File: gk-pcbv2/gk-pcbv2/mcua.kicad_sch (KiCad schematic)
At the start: 23 parts, among them J14 Conn_01x02, SW1 SW_Push, U4 STM32H747BITx, Y1 16MHz, Y2 32.768kHz R26-32.768-12.5

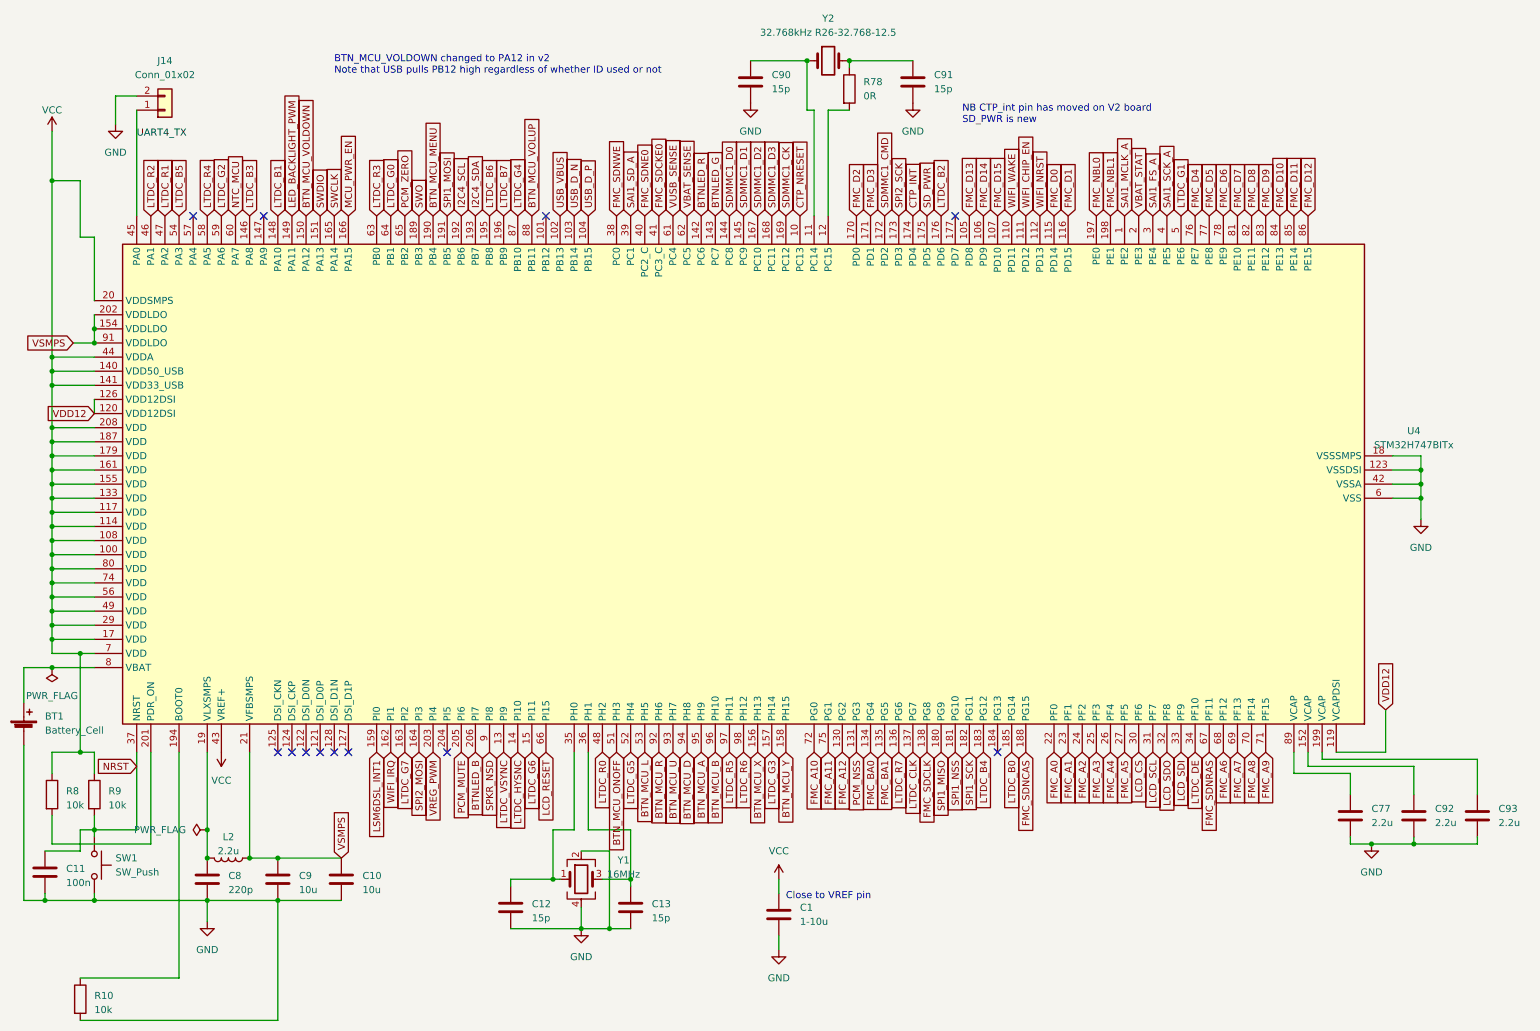
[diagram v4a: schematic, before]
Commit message: PCB updates - add xbox joystick
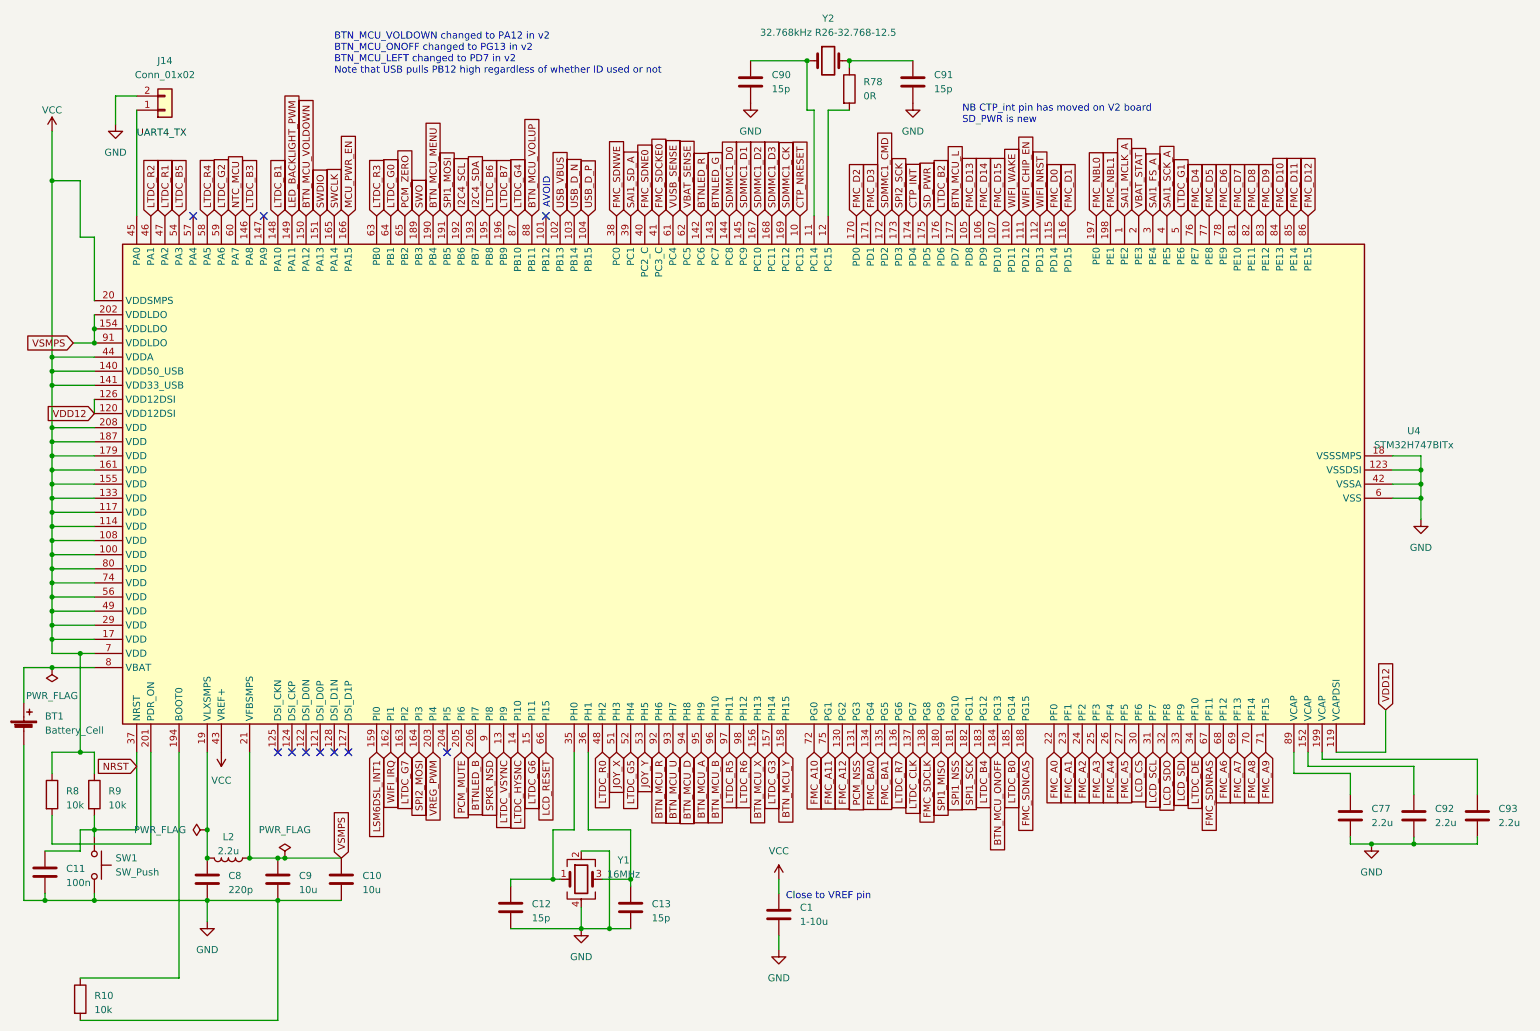
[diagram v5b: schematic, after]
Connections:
- net BTN_MCU_L: now also U4.177 (PD7); no longer U4.53 (PH5)
- net BTN_MCU_ONOFF: now also U4.184 (PG13); no longer U4.51 (PH3)
- new net JOY_X: U4.51 (PH3)
- new net JOY_Y: U4.53 (PH5)
- no-connect marks 12 -> 10
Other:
- note added: "AVOID"
- note added: "BTN_MCU_VOLDOWN changed to PA12 in v2 BTN_MCU_ONOFF changed to PG13 in v2 BTN_MCU_LEFT changed to PD7 in v2 Note that USB pulls PB12 high regardless of whether ID used or not"
- note removed: "BTN_MCU_VOLDOWN changed to PA12 in v2 Note that USB pulls PB12 high regardless of whether ID used or not"
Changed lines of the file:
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@@
   (junction (at 20.32 110.49) (diameter 0) (color 0 0 0 0)
+  )
+  (junction (at 62.23 165.1) (diameter 0) (color 0 0 0 0)
   )
   (junction (at 20.32 115.57) (diameter 0) (color 0 0 0 0)
@@
   (no_connect (at 109.22 49.53))
   (no_connect (at 45.72 49.53))
-  (no_connect (at 190.5 146.05))
   (no_connect (at 63.5 146.05))
   (no_connect (at 66.04 146.05))
@@
   (no_connect (at 58.42 49.53))
   (no_connect (at 60.96 146.05))
-  (no_connect (at 182.88 49.53))
   (wire (pts (xy 31.75 27.94) (xy 31.75 33.02))
     (stroke (width 0) (type default))
@@
     (stroke (width 0) (type default))
   )
+  (wire (pts (xy 62.23 165.1) (xy 72.39 165.1))
+    (stroke (width 0) (type default))
+  )
   (wire (pts (xy 27.94 146.05) (xy 25.4 146.05))
     (stroke (width 0) (type default))
@@
     (stroke (width 0) (type default))
   )
-  (wire (pts (xy 60.96 165.1) (xy 72.39 165.1))
+  (wire (pts (xy 60.96 165.1) (xy 62.23 165.1))
     (stroke (width 0) (type default))
   )
@@
     (effects (font (size 1.27 1.27)) (justify left bottom))
   )
-  (text "BTN_MCU_VOLDOWN changed to PA12 in v2\nNote that USB pulls PB12 high regardless of whether ID used or not"
+  (text "AVOID" (at 110.0906 48.1471 90)
+    (effects (font (size 1.27 1.27)) (justify left bottom))
+  )
+  (text "BTN_MCU_VOLDOWN changed to PA12 in v2\nBTN_MCU_ONOFF changed to PG13 in v2\nBTN_MCU_LEFT changed to PD7 in v2\nNote that USB pulls PB12 high regardless of whether ID used or not"
     (at 71.12 24.13 0)
     (effects (font (size 1.27 1.27)) (justify left bottom))
@@
     )
   )
+  (global_label "JOY_Y" (shape input) (at 127 146.05 270) (fields_autoplaced)
+    (effects (font (size 1.27 1.27)) (justify right))
+    (property "Intersheetrefs" "${INTERSHEET_REFS}" (at 127 154.4781 90)
+      (effects (font (size 1.27 1.27)) (justify right) hide)
+    )
+  )
   (global_label "LTDC_B3" (shape input) (at 55.88 49.53 90) (fields_autoplaced)
     (effects (font (size 1.27 1.27)) (justify left))
@@
     )
   )
+  (global_label "JOY_X" (shape input) (at 121.92 146.05 270) (fields_autoplaced)
+    (effects (font (size 1.27 1.27)) (justify right))
+    (property "Intersheetrefs" "${INTERSHEET_REFS}" (at 121.92 154.599 90)
+      (effects (font (size 1.27 1.27)) (justify right) hide)
+    )
+  )
   (global_label "CTP_INT" (shape input) (at 175.26 49.53 90) (fields_autoplaced)
     (effects (font (size 1.27 1.27)) (justify left))
@@
     )
   )
-  (global_label "BTN_MCU_ONOFF" (shape input) (at 121.92 146.05 270) (fields_autoplaced)
-    (effects (font (size 1.27 1.27)) (justify right))
-    (property "Intersheetrefs" "${INTERSHEET_REFS}" (at 121.92 164.6797 90)
+  (global_label "BTN_MCU_ONOFF" (shape input) (at 190.5 146.05 270) (fields_autoplaced)
+    (effects (font (size 1.27 1.27)) (justify right))
+    (property "Intersheetrefs" "${INTERSHEET_REFS}" (at 190.5 164.6797 90)
       (effects (font (size 1.27 1.27)) (justify right) hide)
     )
@@
     )
   )
-  (global_label "BTN_MCU_L" (shape input) (at 127 146.05 270) (fields_autoplaced)
-    (effects (font (size 1.27 1.27)) (justify right))
-    (property "Intersheetrefs" "${INTERSHEET_REFS}" (at 127 159.5391 90)
-      (effects (font (size 1.27 1.27)) (justify right) hide)
+  (global_label "BTN_MCU_L" (shape input) (at 182.88 49.53 90) (fields_autoplaced)
+    (effects (font (size 1.27 1.27)) (justify left))
+    (property "Intersheetrefs" "${INTERSHEET_REFS}" (at 182.88 35.9615 90)
+      (effects (font (size 1.27 1.27)) (justify left) hide)
     )
   )
@@
         )
       )
+    )
+  )
+  (symbol (lib_id "power:PWR_FLAG") (at 62.23 165.1 0) (unit 1)
+    (in_bom yes) (on_board yes) (dnp no) (fields_autoplaced)
+    (property "Reference" "#FLG010" (at 62.23 163.195 0)
+      (effects (font (size 1.27 1.27)) hide)
+    )
+    (property "Value" "PWR_FLAG" (at 62.23 160.02 0)
+      (effects (font (size 1.27 1.27)))
+    )
+    (property "Footprint" "" (at 62.23 165.1 0)
+      (effects (font (size 1.27 1.27)) hide)
+    )
+    (property "Datasheet" "~" (at 62.23 165.1 0)
+      (effects (font (size 1.27 1.27)) hide)
+    )
+    (pin "1")
+    (instances
+      (project "gk-pcbv2"
+        (path "/08730ac6-6084-459f-bdf1-86b322355ede/d577d9fa-dd9e-43ac-82a3-80fa54936848"
+          (reference "#FLG010") (unit 1)
+        )
+      )

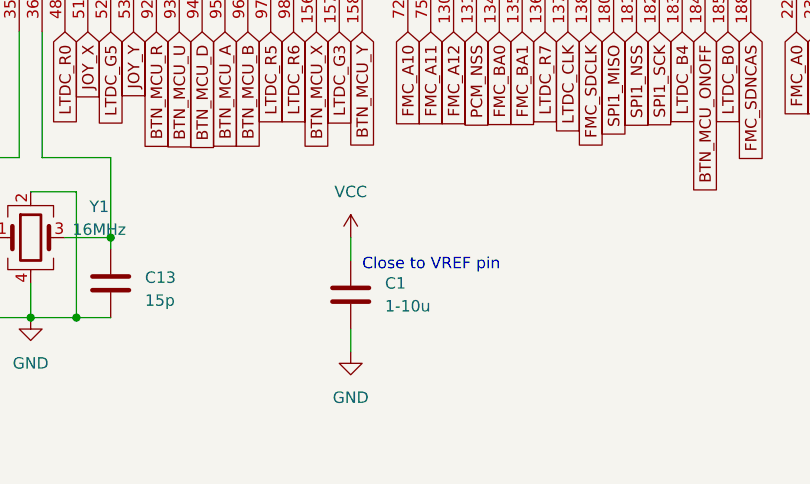
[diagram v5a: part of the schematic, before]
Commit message: experimental v3 pcb with dsi display
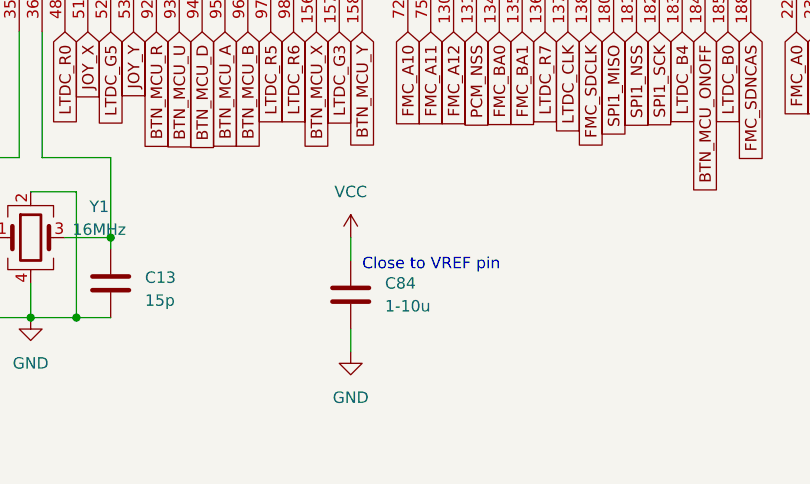
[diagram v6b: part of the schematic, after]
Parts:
- Y2: value 32.768kHz R26-32.768-12.5 -> 32.768kHz R26-32.768-12.5
- renumbered C1 to C84
